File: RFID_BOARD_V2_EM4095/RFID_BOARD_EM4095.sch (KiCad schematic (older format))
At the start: 25 parts, among them J1 CONN_01X05, J2 CONN_01X01, J3 CONN_01X01, U1 EM4095

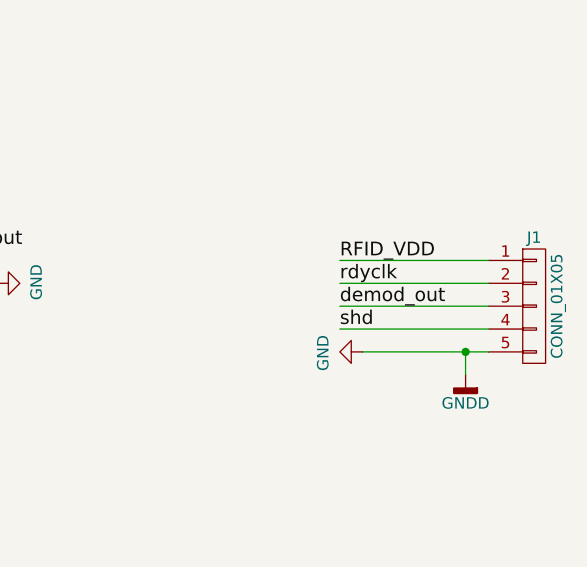
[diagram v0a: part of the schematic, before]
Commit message: second PCB for EM4095 and created fabrication files of main board and corrected holes locations
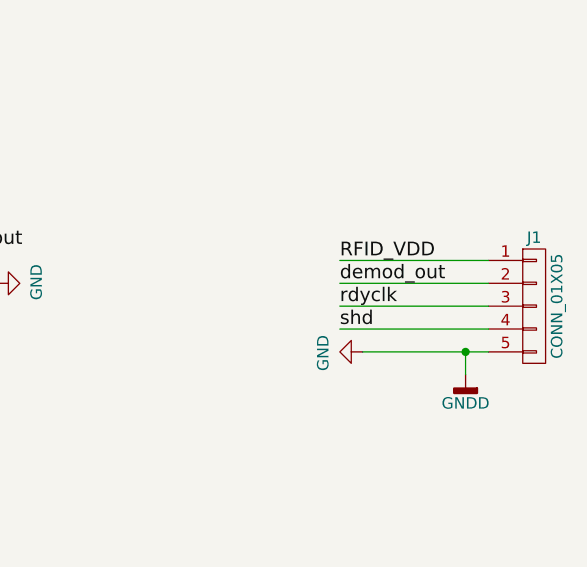
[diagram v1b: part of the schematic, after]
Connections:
- net demod_out: now also J1.2 (P2); no longer J1.3 (P3)
- net rdyclk: now also J1.3 (P3); no longer J1.2 (P2)
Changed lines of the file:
@@
 	1    0    0    -1
 $EndComp
+Text Label 7850 4650 0    60   ~ 0
+rdyclk
 Text Label 7850 4550 0    60   ~ 0
-rdyclk
-Text Label 7850 4650 0    60   ~ 0
 demod_out
 Wire Wire Line

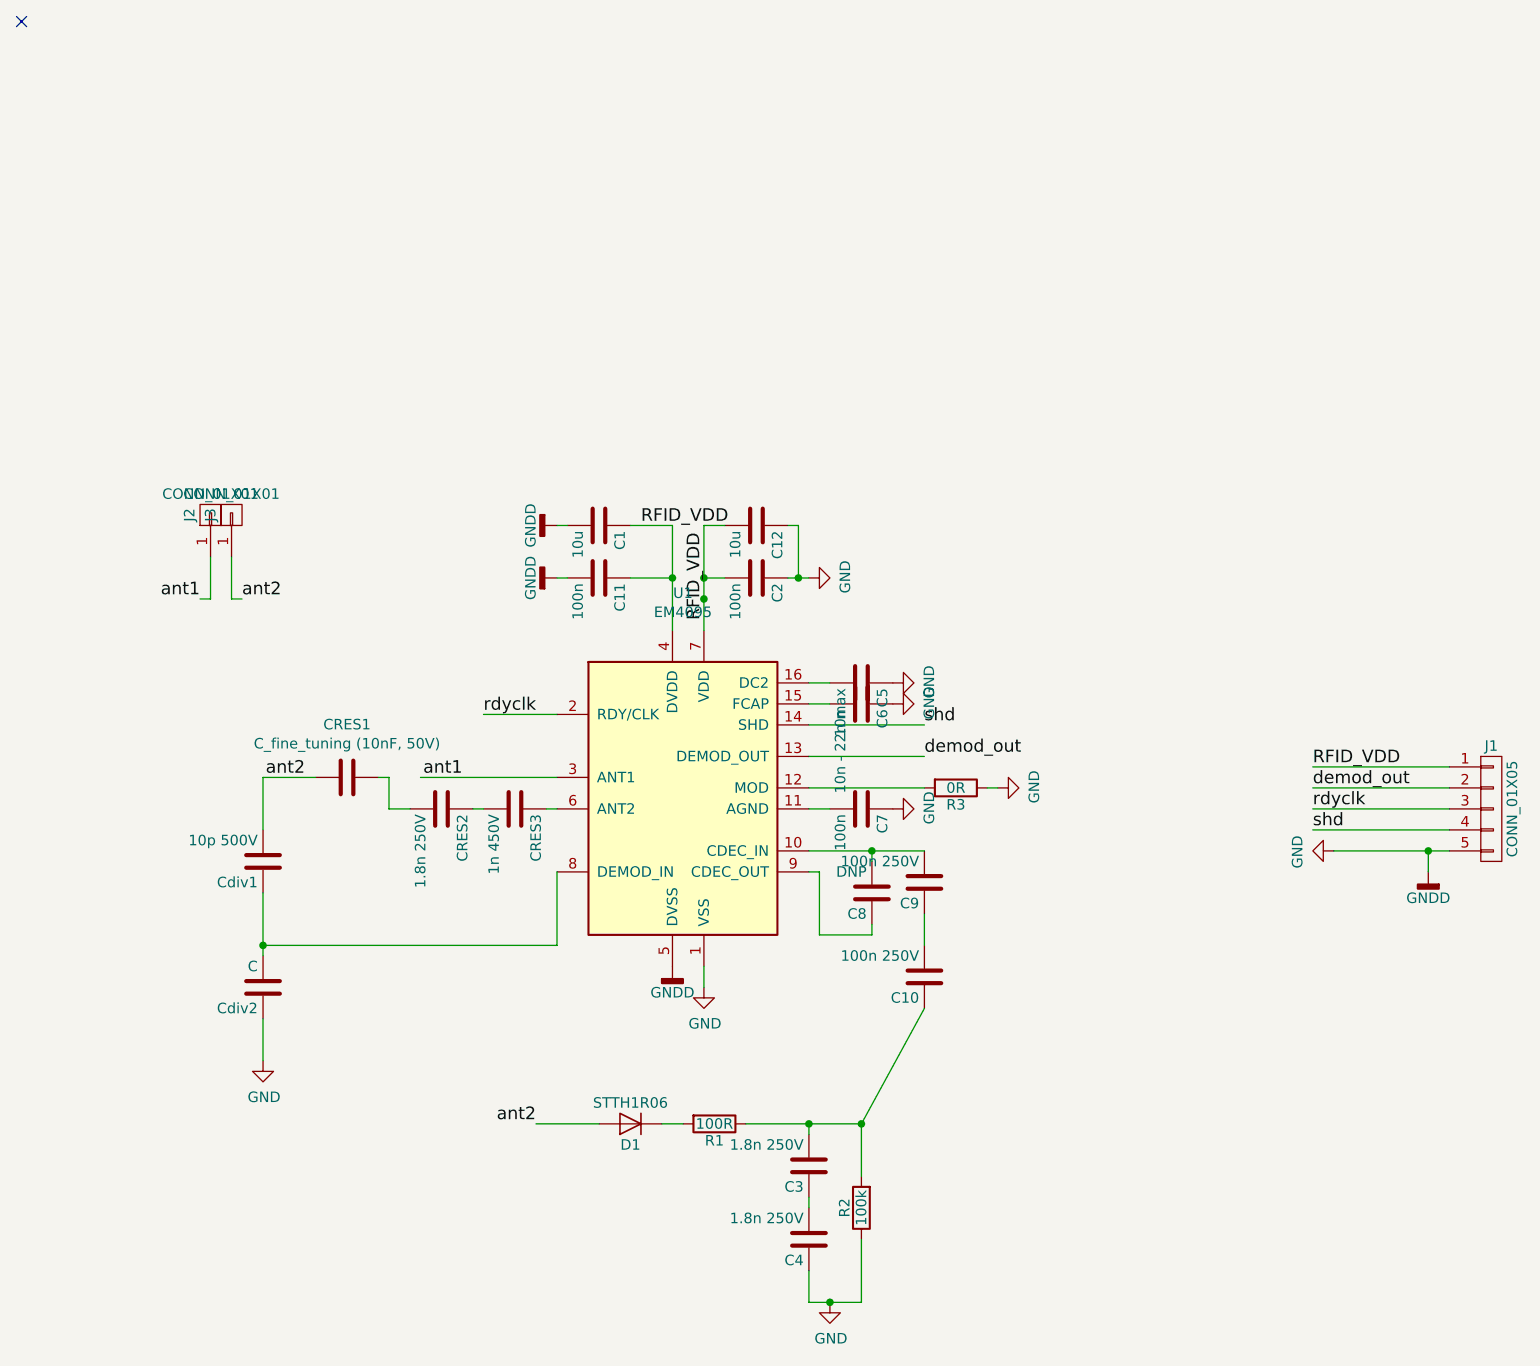
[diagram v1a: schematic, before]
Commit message: annotated schematic with necessary changes to load cell circuit. added pull-ups for enable PMOSes
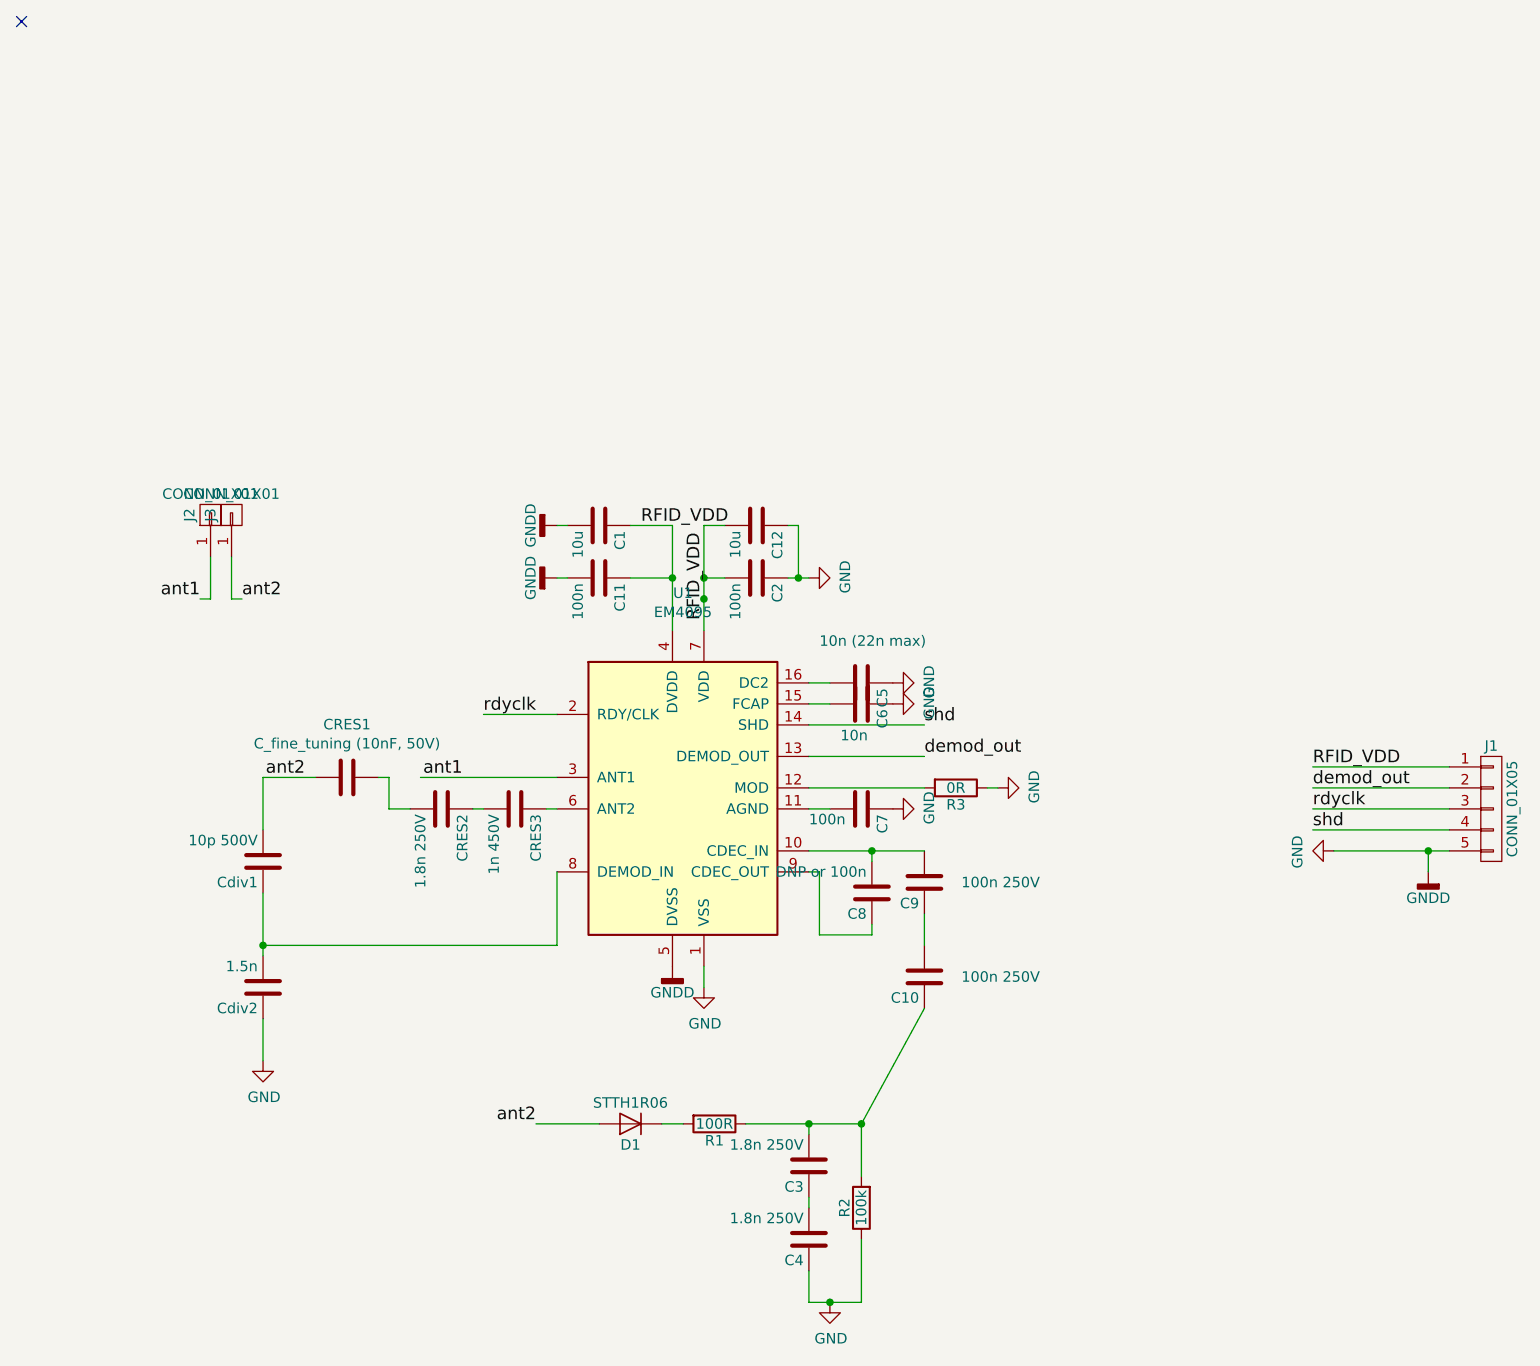
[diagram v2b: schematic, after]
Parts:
- C5: value 10n - 22n max -> 10n (22n max)
- C8: value DNP -> DNP or 100n
- Cdiv2: value C -> 1.5n
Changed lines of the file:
@@
 P 6000 5000
 F 0 "C9" H 6025 5100 50  0000 L CNN
-F 1 "100n 250V" H 6025 4900 50  0000 L CNN
+F 1 "100n 250V" H 5450 5000 50  0000 L CNN
 F 2 "Capacitors_SMD:C_0603" H 6038 4850 50  0001 C CNN
 F 3 "" H 6000 5000 50  0001 C CNN
@@
 P 2850 5500
 F 0 "Cdiv2" H 2875 5600 50  0000 L CNN
-F 1 "C" H 2875 5400 50  0000 L CNN
+F 1 "1.5n" H 2875 5400 50  0000 L CNN
 F 2 "Capacitors_SMD:C_0603" H 2888 5350 50  0001 C CNN
 F 3 "" H 2850 5500 50  0001 C CNN
@@
 demod_out
 Wire Wire Line
-	4950 3300 4950 3800
+	4950 3300 4950 3550
+Wire Wire Line
+	4950 3550 4950 3650
+Wire Wire Line
+	4950 3650 4950 3800
 Text Label 7850 4450 0    60   ~ 0
 RFID_VDD
@@
 $EndComp
 Wire Wire Line
-	7950 4850 8500 4850
+	7950 4850 8400 4850
+Wire Wire Line
+	8400 4850 8500 4850
 Wire Wire Line
 	8500 4750 7850 4750
@@
 	4950 5500 4950 5400
 Wire Wire Line
-	4800 3300 4800 3800
+	4800 3300 4800 3550
+Wire Wire Line
+	4800 3550 4800 3800
 Connection ~ 4950 3650
 $Comp
@@
 P 5700 4050
 F 0 "C5" H 5725 4150 50  0000 L CNN
-F 1 "10n - 22n max" H 5725 3950 50  0000 L CNN
+F 1 "10n  (22n max)" V 5500 3850 50  0000 L CNN
 F 2 "Capacitors_SMD:C_0603" H 5738 3900 50  0001 C CNN
 F 3 "" H 5700 4050 50  0001 C CNN
@@
 P 5700 4150
 F 0 "C6" H 5725 4250 50  0000 L CNN
-F 1 "10n" H 5725 4050 50  0000 L CNN
+F 1 "10n" V 5850 4050 50  0000 L CNN
 F 2 "Capacitors_SMD:C_0603" H 5738 4000 50  0001 C CNN
 F 3 "" H 5700 4150 50  0001 C CNN
@@
 P 5700 4650
 F 0 "C7" H 5725 4750 50  0000 L CNN
-F 1 "100n" H 5725 4550 50  0000 L CNN
+F 1 "100n" V 5750 4400 50  0000 L CNN
 F 2 "Capacitors_SMD:C_0603" H 5738 4500 50  0001 C CNN
 F 3 "" H 5700 4650 50  0001 C CNN
@@
 	5550 4650 5450 4650
 Wire Wire Line
-	5450 4850 6000 4850
+	5450 4850 5750 4850
+Wire Wire Line
+	5750 4850 6000 4850
 Wire Wire Line
 	4250 4200 3900 4200
@@
 rdyclk
 Wire Wire Line
-	2850 5050 2850 5350
+	2850 5050 2850 5300
+Wire Wire Line
+	2850 5300 2850 5350
 Wire Wire Line
 	2850 5650 2850 5850
@@
 $EndComp
 Wire Wire Line
-	5350 3550 5450 3550
+	5350 3550 5400 3550
+Wire Wire Line
+	5400 3550 5450 3550
 $Comp
 L EM4095 U1
@@
 	4850 6150 4750 6150
 Wire Wire Line
-	5150 6150 5700 6150
+	5150 6150 5450 6150
+Wire Wire Line
+	5450 6150 5700 6150
 $Comp
 L R R2
@@
 P 6000 5450
 F 0 "C10" H 6025 5550 50  0000 L CNN
-F 1 "100n 250V" H 6025 5350 50  0000 L CNN
+F 1 "100n 250V" H 5450 5450 50  0000 L CNN
 F 2 "Capacitors_SMD:C_0603" H 6038 5300 50  0001 C CNN
 F 3 "" H 6000 5450 50  0001 C CNN
@@
 	5450 6850 5450 7000
 Wire Wire Line
-	5450 7000 5700 7000
+	5450 7000 5550 7000
+Wire Wire Line
+	5550 7000 5700 7000
 Wire Wire Line
 	5700 7000 5700 6700
@@
 P 5750 5050
 F 0 "C8" H 5775 5150 50  0000 L CNN
-F 1 "DNP" H 5775 4950 50  0000 L CNN
+F 1 "DNP or 100n" H 5775 4950 50  0000 L CNN
 F 2 "Capacitors_SMD:C_0603" H 5788 4900 50  0001 C CNN
 F 3 "DNP" H 5750 5050 50  0001 C CNN

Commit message: TAPEOUT second batch nestbox main + EM pcb. added pull-ups, corrected pmos of load cell, WIFI AND SDCARD ENABLE PMOS ARE STILL WRONGLY ORIENTED
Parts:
- C1, C12: footprint Capacitors_SMD:C_0603 -> Capacitors_SMD:C_0805
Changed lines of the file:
@@
 demod_out
 Wire Wire Line
-	4950 3300 4950 3550
-Wire Wire Line
-	4950 3550 4950 3650
-Wire Wire Line
-	4950 3650 4950 3800
+	4950 3300 4950 3800
 Text Label 7850 4450 0    60   ~ 0
 RFID_VDD
@@
 $EndComp
 Wire Wire Line
-	7950 4850 8400 4850
-Wire Wire Line
-	8400 4850 8500 4850
+	7950 4850 8500 4850
 Wire Wire Line
 	8500 4750 7850 4750
@@
 	4950 5500 4950 5400
 Wire Wire Line
-	4800 3300 4800 3550
-Wire Wire Line
-	4800 3550 4800 3800
+	4800 3300 4800 3800
 Connection ~ 4950 3650
 $Comp
@@
 	5550 4650 5450 4650
 Wire Wire Line
-	5450 4850 5750 4850
-Wire Wire Line
-	5750 4850 6000 4850
+	5450 4850 6000 4850
 Wire Wire Line
 	4250 4200 3900 4200
@@
 rdyclk
 Wire Wire Line
-	2850 5050 2850 5300
-Wire Wire Line
-	2850 5300 2850 5350
+	2850 5050 2850 5350
 Wire Wire Line
 	2850 5650 2850 5850
@@
 F 0 "C1" H 4475 3400 50  0000 L CNN
 F 1 "10u" H 4475 3200 50  0000 L CNN
-F 2 "Capacitors_SMD:C_0603" H 4488 3150 50  0001 C CNN
+F 2 "Capacitors_SMD:C_0805" H 4488 3150 50  0001 C CNN
 F 3 "" H 4450 3300 50  0001 C CNN
 	1    4450 3300
@@
 $EndComp
 Wire Wire Line
-	5350 3550 5400 3550
-Wire Wire Line
-	5400 3550 5450 3550
+	5350 3550 5450 3550
 $Comp
 L EM4095 U1
@@
 	4850 6150 4750 6150
 Wire Wire Line
-	5150 6150 5450 6150
-Wire Wire Line
-	5450 6150 5700 6150
+	5150 6150 5700 6150
 $Comp
 L R R2
@@
 	5450 6850 5450 7000
 Wire Wire Line
-	5450 7000 5550 7000
-Wire Wire Line
-	5550 7000 5700 7000
+	5450 7000 5700 7000
 Wire Wire Line
 	5700 7000 5700 6700
@@
 F 0 "C12" H 5225 3400 50  0000 L CNN
 F 1 "10u" H 5225 3200 50  0000 L CNN
-F 2 "Capacitors_SMD:C_0603" H 5238 3150 50  0001 C CNN
+F 2 "Capacitors_SMD:C_0805" H 5238 3150 50  0001 C CNN
 F 3 "" H 5200 3300 50  0001 C CNN
 	1    5200 3300
